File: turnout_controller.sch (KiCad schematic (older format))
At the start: 29 parts, among them J1 DCC_A, J2 DCC_B, J3 PROG, J4 MOT_CNTL, J5 MOT_POWER, J6 MOT_GND, J7 LED_1, J8 LED_2, SW1 SW_Push, SW2 SW_Push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

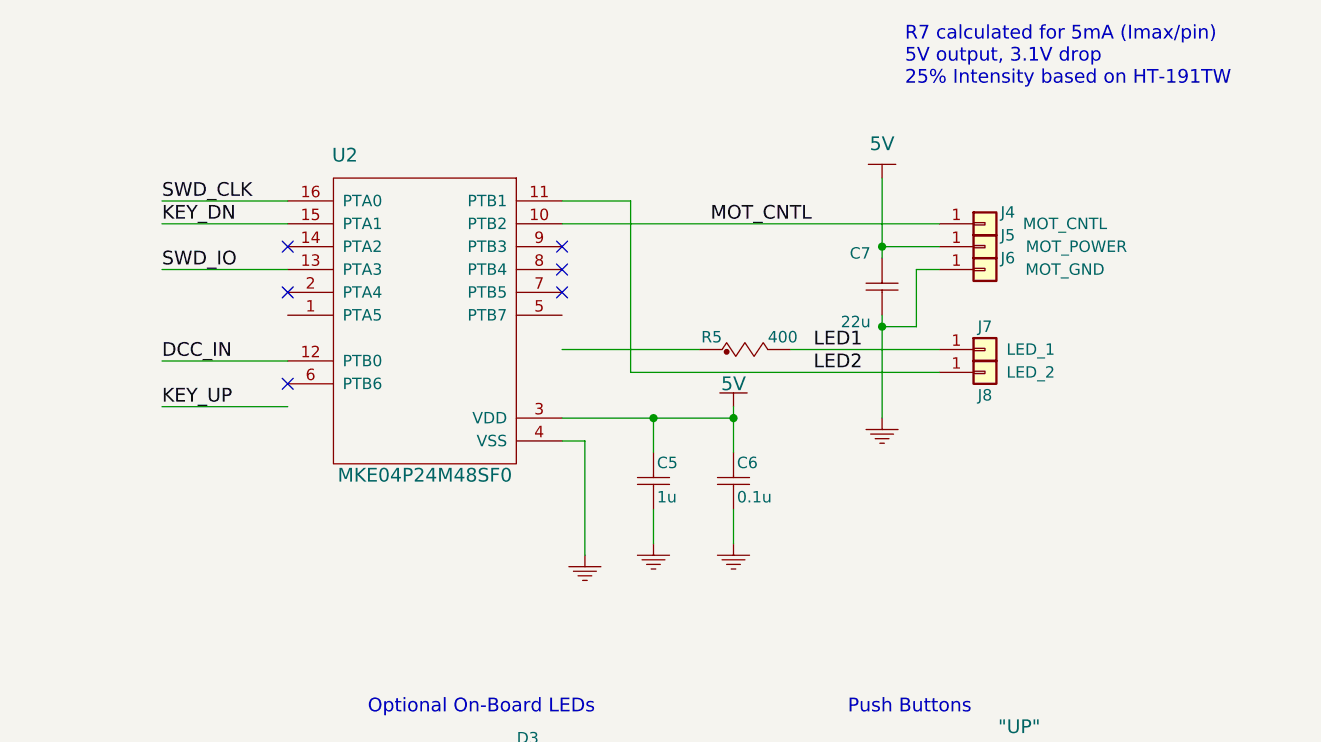
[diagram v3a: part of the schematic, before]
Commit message: Updated schematics and board layout to fix LED issue
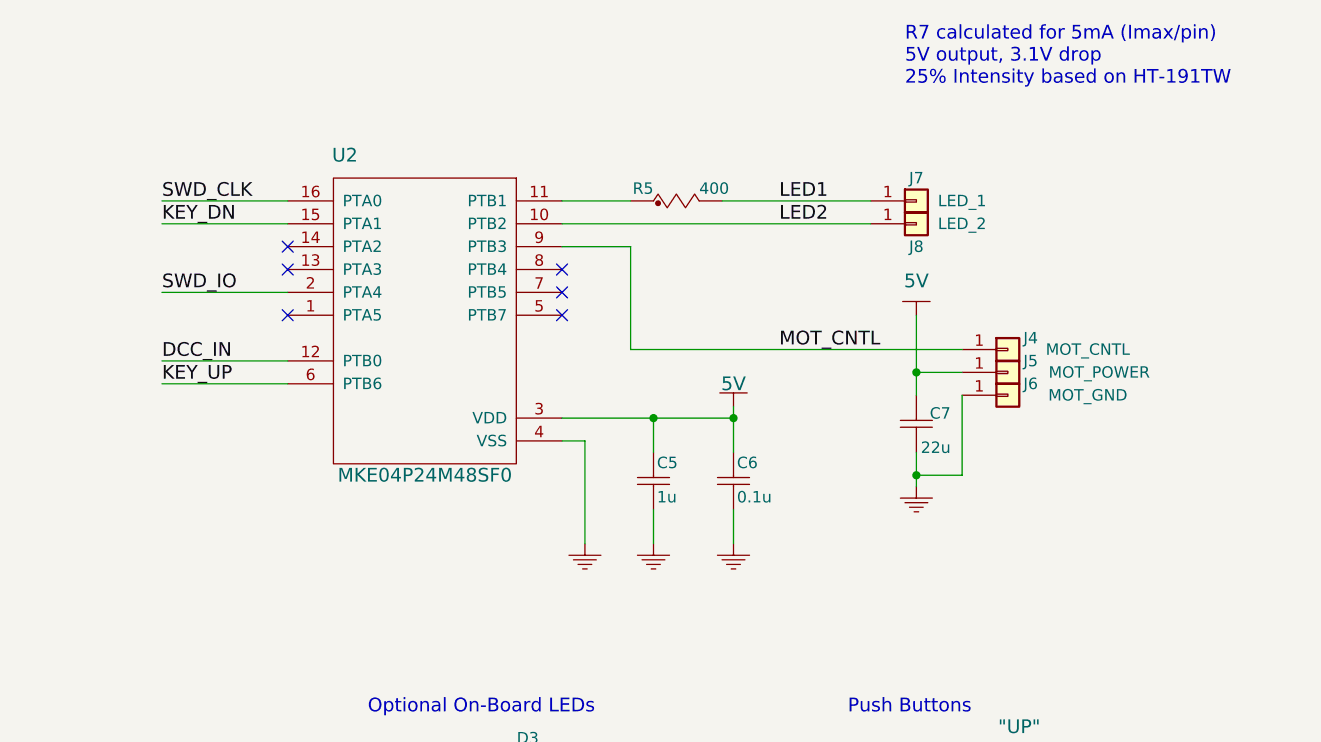
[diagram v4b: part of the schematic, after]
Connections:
- wire segments 82 -> 81
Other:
- moved on the sheet: C7, J4, J5, J6, J7, J8, R5
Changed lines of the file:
@@
 L 5V #PWR02
 U 1 1 59FFF089
-P 9350 1250
-F 0 "#PWR02" H 9350 1350 40  0001 C CNN
-F 1 "5V" H 9350 1400 60  0000 C CNN
-F 2 "" H 9350 1250 60  0000 C CNN
-F 3 "" H 9350 1250 60  0000 C CNN
-	1    9350 1250
+P 9500 1850
+F 0 "#PWR02" H 9500 1950 40  0001 C CNN
+F 1 "5V" H 9500 2000 60  0000 C CNN
+F 2 "" H 9500 1850 60  0000 C CNN
+F 3 "" H 9500 1850 60  0000 C CNN
+	1    9500 1850
 	1    0    0    -1
 $EndComp
@@
 L RES R5
 U 1 1 5A1324E5
-P 8550 2050
-F 0 "R5" H 8650 2125 50  0000 R BNN
-F 1 "400" H 8850 2125 50  0000 L BNN
-F 2 "Resistors_SMD:R_0603_HandSoldering" H 8650 2000 40  0001 L BNN
-F 3 "" H 8550 2050 60  0000 C CNN
-F 4 "PAT0603E4000BST1" H 8550 2050 60  0001 C CNN "MFG P/N"
-F 5 "Value" H 8550 2050 60  0001 C CNN "MFG"
-F 6 "Value" H 8550 2050 60  0001 C CNN "P/N"
-	1    8550 2050
+P 8250 1400
+F 0 "R5" H 8350 1475 50  0000 R BNN
+F 1 "400" H 8550 1475 50  0000 L BNN
+F 2 "Resistors_SMD:R_0603_HandSoldering" H 8350 1350 40  0001 L BNN
+F 3 "" H 8250 1400 60  0000 C CNN
+F 4 "PAT0603E4000BST1" H 8250 1400 60  0001 C CNN "MFG P/N"
+F 5 "Value" H 8250 1400 60  0001 C CNN "MFG"
+F 6 "Value" H 8250 1400 60  0001 C CNN "P/N"
+	1    8250 1400
 	1    0    0    -1
 $EndComp
@@
 L GND_ #PWR04
 U 1 1 5A143353
-P 8050 2950
-F 0 "#PWR04" H 8150 3050 30  0001 C CNN
-F 1 "GND_" H 8050 2850 30  0001 C CNN
-F 2 "" H 8050 2950 60  0000 C CNN
-F 3 "" H 8050 2950 60  0000 C CNN
-	1    8050 2950
+P 8050 2900
+F 0 "#PWR04" H 8150 3000 30  0001 C CNN
+F 1 "GND_" H 8050 2800 30  0001 C CNN
+F 2 "" H 8050 2900 60  0000 C CNN
+F 3 "" H 8050 2900 60  0000 C CNN
+	1    8050 2900
 	1    0    0    -1
 $EndComp
@@
 L GND_ #PWR07
 U 1 1 5A1435B0
-P 9350 2350
-F 0 "#PWR07" H 9450 2450 30  0001 C CNN
-F 1 "GND_" H 9350 2250 30  0001 C CNN
-F 2 "" H 9350 2350 60  0000 C CNN
-F 3 "" H 9350 2350 60  0000 C CNN
-	1    9350 2350
+P 9500 2650
+F 0 "#PWR07" H 9600 2750 30  0001 C CNN
+F 1 "GND_" H 9500 2550 30  0001 C CNN
+F 2 "" H 9500 2650 60  0000 C CNN
+F 3 "" H 9500 2650 60  0000 C CNN
+	1    9500 2650
 	1    0    0    -1
 $EndComp
@@
 L CAP_NP C7
 U 1 1 5A1B4827
-P 9350 1600
-F 0 "C7" H 9400 1550 50  0000 L BNN
-F 1 "22u" H 9400 1850 50  0000 L BNN
-F 2 "Capacitors_SMD:C_0603_HandSoldering" H 9425 1500 40  0001 L BNN
-F 3 "" H 9350 1600 60  0000 C CNN
-F 4 "GRT188R60J226ME13D" H 9350 1600 60  0001 C CNN "MFG P/N"
-F 5 "6.3" H 9450 1550 40  0001 L BNN "Voltage"
-	1    9350 1600
+P 9500 2200
+F 0 "C7" H 9350 2250 50  0000 L BNN
+F 1 "22u" H 9350 2400 50  0000 L BNN
+F 2 "Capacitors_SMD:C_0603_HandSoldering" H 9575 2100 40  0001 L BNN
+F 3 "" H 9500 2200 60  0000 C CNN
+F 4 "GRT188R60J226ME13D" H 9500 2200 60  0001 C CNN "MFG P/N"
+F 5 "6.3" H 9600 2150 40  0001 L BNN "Voltage"
+	1    9500 2200
 	-1   0    0    1
 $EndComp
@@
 	1    0    0    -1
 $EndComp
-NoConn ~ 6750 2150
 NoConn ~ 7950 1750
 NoConn ~ 6750 1550
-Text Label 6200 2250 0    60   ~ 0
+Text Label 6200 2150 0    60   ~ 0
 KEY_UP
 Text Label 6200 1450 0    60   ~ 0
@@
 Text Label 6200 1350 0    60   ~ 0
 SWD_CLK
-NoConn ~ 6750 1750
-Text Label 6200 1650 0    60   ~ 0
+Text Label 6200 1750 0    60   ~ 0
 SWD_IO
 Text Label 7650 5400 0    60   ~ 0
@@
 Text Notes 7100 3600 0    60   ~ 0
 Optional On-Board LEDs
-Text Label 9050 2000 0    60   ~ 0
+Text Label 8900 1350 0    60   ~ 0
 LED1
-Text Label 9050 2100 0    60   ~ 0
+Text Label 8900 1450 0    60   ~ 0
 LED2
 Text Label 7100 4000 0    60   ~ 0
@@
 L Conn_01x01 J4
 U 1 1 5AB2F44B
-P 9800 1450
-F 0 "J4" H 9900 1500 50  0000 C CNN
-F 1 "MOT_CNTL" H 10150 1450 50  0000 C CNN
-F 2 "half-connectors:Socket_Strip_Straight_1x01_Pitch1.27mm_at_edge" H 9800 1450 50  0001 C CNN
-F 3 "" H 9800 1450 50  0001 C CNN
-	1    9800 1450
+P 9900 2000
+F 0 "J4" H 10000 2050 50  0000 C CNN
+F 1 "MOT_CNTL" H 10250 2000 50  0000 C CNN
+F 2 "half-connectors:Socket_Strip_Straight_1x01_Pitch1.27mm_at_edge" H 9900 2000 50  0001 C CNN
+F 3 "" H 9900 2000 50  0001 C CNN
+	1    9900 2000
 	1    0    0    -1
 $EndComp
@@
 L Conn_01x01 J5
 U 1 1 5AB2F4C5
-P 9800 1550
-F 0 "J5" H 9900 1600 50  0000 C CNN
-F 1 "MOT_POWER" H 10200 1550 50  0000 C CNN
-F 2 "half-connectors:Socket_Strip_Straight_1x01_Pitch1.27mm_at_edge" H 9800 1550 50  0001 C CNN
-F 3 "" H 9800 1550 50  0001 C CNN
-	1    9800 1550
+P 9900 2100
+F 0 "J5" H 10000 2150 50  0000 C CNN
+F 1 "MOT_POWER" H 10300 2100 50  0000 C CNN
+F 2 "half-connectors:Socket_Strip_Straight_1x01_Pitch1.27mm_at_edge" H 9900 2100 50  0001 C CNN
+F 3 "" H 9900 2100 50  0001 C CNN
+	1    9900 2100
 	1    0    0    -1
 $EndComp
@@
 L Conn_01x01 J6
 U 1 1 5AB2F530
-P 9800 1650
-F 0 "J6" H 9900 1700 50  0000 C CNN
-F 1 "MOT_GND" H 10150 1650 50  0000 C CNN
-F 2 "half-connectors:Socket_Strip_Straight_1x01_Pitch1.27mm_at_edge" H 9800 1650 50  0001 C CNN
-F 3 "" H 9800 1650 50  0001 C CNN
-	1    9800 1650
+P 9900 2200
+F 0 "J6" H 10000 2250 50  0000 C CNN
+F 1 "MOT_GND" H 10250 2200 50  0000 C CNN
+F 2 "half-connectors:Socket_Strip_Straight_1x01_Pitch1.27mm_at_edge" H 9900 2200 50  0001 C CNN
+F 3 "" H 9900 2200 50  0001 C CNN
+	1    9900 2200
 	1    0    0    -1
 $EndComp
@@
 L Conn_01x01 J7
 U 1 1 5AB2F944
-P 9800 2000
-F 0 "J7" H 9800 2100 50  0000 C CNN
-F 1 "LED_1" H 10000 2000 50  0000 C CNN
-F 2 "half-connectors:Socket_Strip_Straight_1x01_Pitch1.27mm_at_edge" H 9800 2000 50  0001 C CNN
-F 3 "" H 9800 2000 50  0001 C CNN
-	1    9800 2000
+P 9500 1350
+F 0 "J7" H 9500 1450 50  0000 C CNN
+F 1 "LED_1" H 9700 1350 50  0000 C CNN
+F 2 "half-connectors:Socket_Strip_Straight_1x01_Pitch1.27mm_at_edge" H 9500 1350 50  0001 C CNN
+F 3 "" H 9500 1350 50  0001 C CNN
+	1    9500 1350
 	1    0    0    -1
 $EndComp
@@
 L Conn_01x01 J8
 U 1 1 5AB2FA1F
-P 9800 2100
-F 0 "J8" H 9800 2000 50  0000 C CNN
-F 1 "LED_2" H 10000 2100 50  0000 C CNN
-F 2 "half-connectors:Socket_Strip_Straight_1x01_Pitch1.27mm_at_edge" H 9800 2100 50  0001 C CNN
-F 3 "" H 9800 2100 50  0001 C CNN
-	1    9800 2100
+P 9500 1450
+F 0 "J8" H 9500 1350 50  0000 C CNN
+F 1 "LED_2" H 9700 1450 50  0000 C CNN
+F 2 "half-connectors:Socket_Strip_Straight_1x01_Pitch1.27mm_at_edge" H 9500 1450 50  0001 C CNN
+F 3 "" H 9500 1450 50  0001 C CNN
+	1    9500 1450
 	1    0    0    -1
 $EndComp
@@
 	7950 2400 8050 2400
 Wire Wire Line
-	8950 2000 9600 2000
-Wire Wire Line
 	3850 1350 3850 1800
 Connection ~ 3850 1650
@@
 Connection ~ 2200 3150
 Wire Wire Line
-	8050 2400 8050 2900
+	8050 2400 8050 2850
 Wire Wire Line
 	8350 2700 8350 2850
 Wire Wire Line
 	8700 2700 8700 2850
-Wire Wire Line
-	9350 1850 9350 2300
-Wire Wire Line
-	9500 1650 9600 1650
-Wire Wire Line
-	9350 1900 9500 1900
-Wire Wire Line
-	9500 1900 9500 1650
-Connection ~ 9350 1900
 Wire Wire Line
 	6200 1450 6750 1450
@@
 	3450 2200 3850 2200
 Connection ~ 3850 2200
-Wire Wire Line
-	9350 1250 9350 1600
-Wire Wire Line
-	9600 1550 9350 1550
-Connection ~ 9350 1550
 Wire Wire Line
 	7450 5300 7950 5300
@@
 Wire Wire Line
 	6200 1350 6750 1350
-Wire Wire Line
-	6750 2050 6200 2050
-Wire Wire Line
-	6750 2250 6200 2250
-Wire Wire Line
-	7950 1350 8250 1350
-Wire Wire Line
-	6750 1650 6200 1650
-Text Label 8600 1450 0    60   ~ 0
+Text Label 8900 2000 0    60   ~ 0
 MOT_CNTL
-Wire Wire Line
-	7950 1450 9600 1450
-NoConn ~ 7950 1550
-NoConn ~ 7950 1650
-Wire Wire Line
-	7950 2000 8550 2000
-Wire Wire Line
-	8250 1350 8250 2100
-Wire Wire Line
-	8250 2100 9600 2100
 Wire Wire Line
 	7950 2300 8700 2300
@@
 	8700 2250 8700 2450
 Connection ~ 8700 2300
+Wire Wire Line
+	7950 1450 9300 1450
+NoConn ~ 6750 1850
+Wire Wire Line
+	6750 2050 6200 2050
+Wire Wire Line
+	6750 2150 6200 2150
+Wire Wire Line
+	6200 1750 6750 1750
+NoConn ~ 6750 1650
+Wire Wire Line
+	7950 1350 8250 1350
+Wire Wire Line
+	8650 1350 9300 1350
+NoConn ~ 7950 1650
+NoConn ~ 7950 1850
+Wire Wire Line
+	7950 1550 8250 1550
+Wire Wire Line
+	8250 1550 8250 2000
+Wire Wire Line
+	9700 2100 9500 2100
+Wire Wire Line
+	9500 1850 9500 2200
+Wire Wire Line
+	9700 2200 9700 2550
+Connection ~ 9500 2100
+Wire Wire Line
+	9500 2450 9500 2600
+Wire Wire Line
+	9700 2550 9500 2550
+Connection ~ 9500 2550
+Wire Wire Line
+	8250 2000 9700 2000
 $EndSCHEMATC
